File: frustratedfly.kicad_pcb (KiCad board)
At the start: 2 copper layers, 210.2 x 107 mm, 73 parts, among them SW1 CPG1316S, SW10 CPG1316S, SW11 CPG1316S, SW12 CPG1316S, SW13 CPG1316S, SW14 CPG1316S, SW15 CPG1316S, SW16 CPG1316S, SW17 CPG1316S, SW18 CPG1316S, SW19 CPG1316S, SW2 CPG1316S, SW20 CPG1316S, SW21 CPG1316S, SW22 CPG1316S, SW23 CPG1316S, SW24 CPG1316S, SW25 CPG1316S, SW26 CPG1316S, SW27 CPG1316S, SW28 CPG1316S, SW29 CPG1316S, SW3 CPG1316S, SW30 CPG1316S, SW31 CPG1316S, SW32 CPG1316S, SW33 CPG1316S, SW34 CPG1316S, SW35 CPG1316S, SW36 CPG1316S, SW4 CPG1316S, SW5 CPG1316S, SW6 CPG1316S, SW7 CPG1316S, SW8 CPG1316S, SW9 CPG1316S

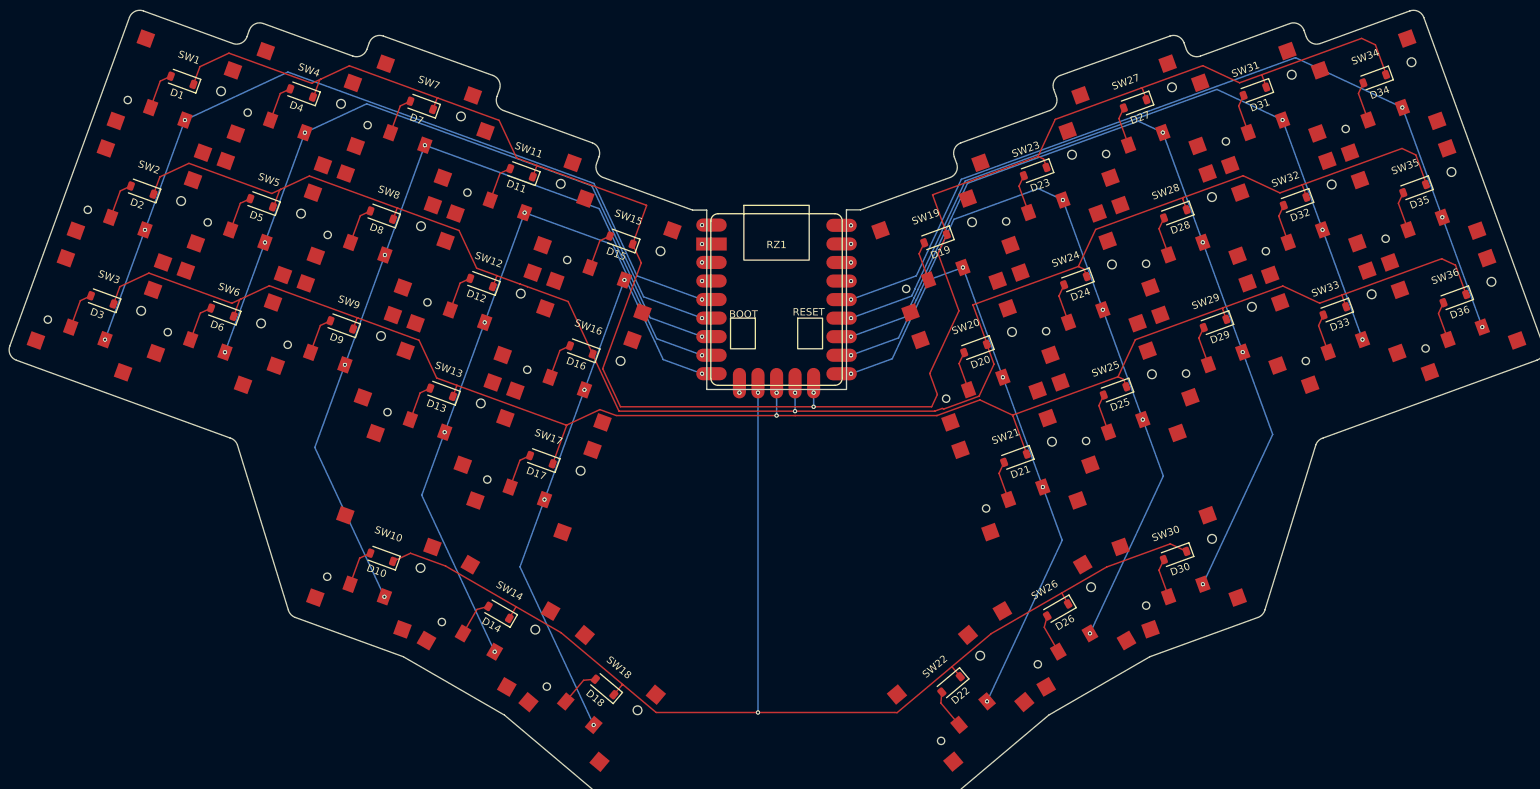
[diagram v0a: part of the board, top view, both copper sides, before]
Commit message: Added project specific kicad libs
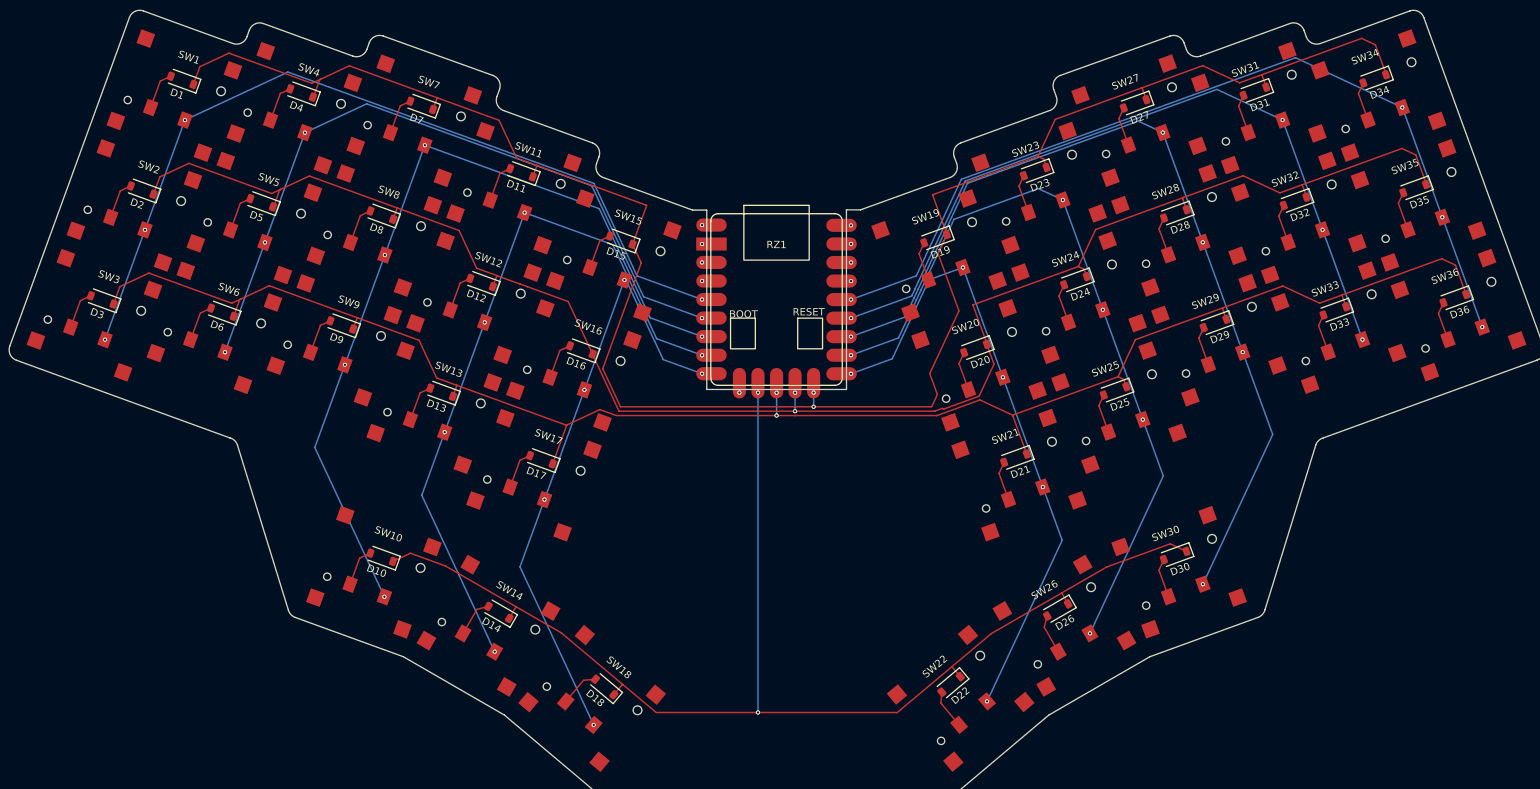
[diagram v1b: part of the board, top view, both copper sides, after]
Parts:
- RZ1: footprint Keyboard_stuff:RP2040_Zero_cutout -> frustratedfly:RP2040_Zero_cutout
- SW1, SW10, SW11, SW12, SW13, SW14, SW15, SW16, SW17, SW18, SW19, SW2, SW20, SW21, SW22, SW23, SW24, SW25, SW26, SW27, SW28, SW29, SW3, SW30, SW31, SW32, SW33, SW34, SW35, SW36, SW4, SW5, SW6, SW7, SW8, SW9: footprint Keyboard_stuff:CPG1316S01D02_mikeholscher_w_ref -> frustratedfly:CPG1316S01D02_mikeholscher_w_ref

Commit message: 17mm ctc spacing
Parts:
- moved SW3 31.2 mm to (35.3, 89.1)
- moved D3 31.2 mm to (36.3, 87.0)
- moved D2 31.0 mm to (42.1, 71.1)
- moved SW2 31.0 mm to (41.1, 73.2)
- moved D1 30.7 mm to (48.0, 55.1)
- moved SW1 30.7 mm to (46.9, 57.2)
- moved D6 30.3 mm to (53.8, 88.9)
- moved SW6 30.2 mm to (52.7, 91.0)
- moved SW5 30.0 mm to (58.5, 75.0)
- moved D5 29.9 mm to (59.6, 72.9)
- moved SW4 29.7 mm to (64.3, 59.0)
- moved D4 29.7 mm to (65.4, 56.9)
- moved SW9 29.2 mm to (70.1, 92.8)
- moved D9 29.2 mm to (71.2, 90.7)
- moved SW8 29.0 mm to (75.9, 76.8)
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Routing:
- net Net-(D13-K): track 231.5 -> 250.9 mm
- net Net-(D10-K): track 173.9 -> 191.4 mm
- net Net-(RZ1-Pad8): track 87.0 -> 103.6 mm
- net Net-(RZ1-Pad14): track 83.6 -> 99.9 mm
- net Net-(RZ1-Pad7): track 104.9 -> 119.9 mm
- net Net-(RZ1-Pad15): track 98.6 -> 113.1 mm
- net Net-(D12-K): track 231.3 -> 245.6 mm
- net Net-(D1-K): track 260.0 -> 273.1 mm
- net Net-(RZ1-Pad26): track 116.2 -> 125.9 mm
- net Net-(RZ1-Pad28): track 115.6 -> 123.6 mm
- net Net-(RZ1-Pad4): track 121.0 -> 128.8 mm
- net Net-(RZ1-Pad6): track 123.3 -> 131.1 mm
- net Net-(RZ1-Pad27): track 99.4 -> 106.4 mm
- net Net-(RZ1-Pad5): track 104.8 -> 111.6 mm
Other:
- board size 210.2 x 107 mm -> 226.9 x 114.6 mm
- board text removed: "FrustratedFly qwelyt v1.0"
- board text removed: "JLCJLCJLCJLC"
